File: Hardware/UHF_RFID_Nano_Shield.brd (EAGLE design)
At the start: 77.5 x 53.3 mm, 35 parts, among them J2 FTDI, J3 JST, J4 U.FL, J5 Extra, J6 Screw Terminal, J7 GPIOs, U1 Nano, U2 TXB0104, U3 TVS_DIODE_ARRAY

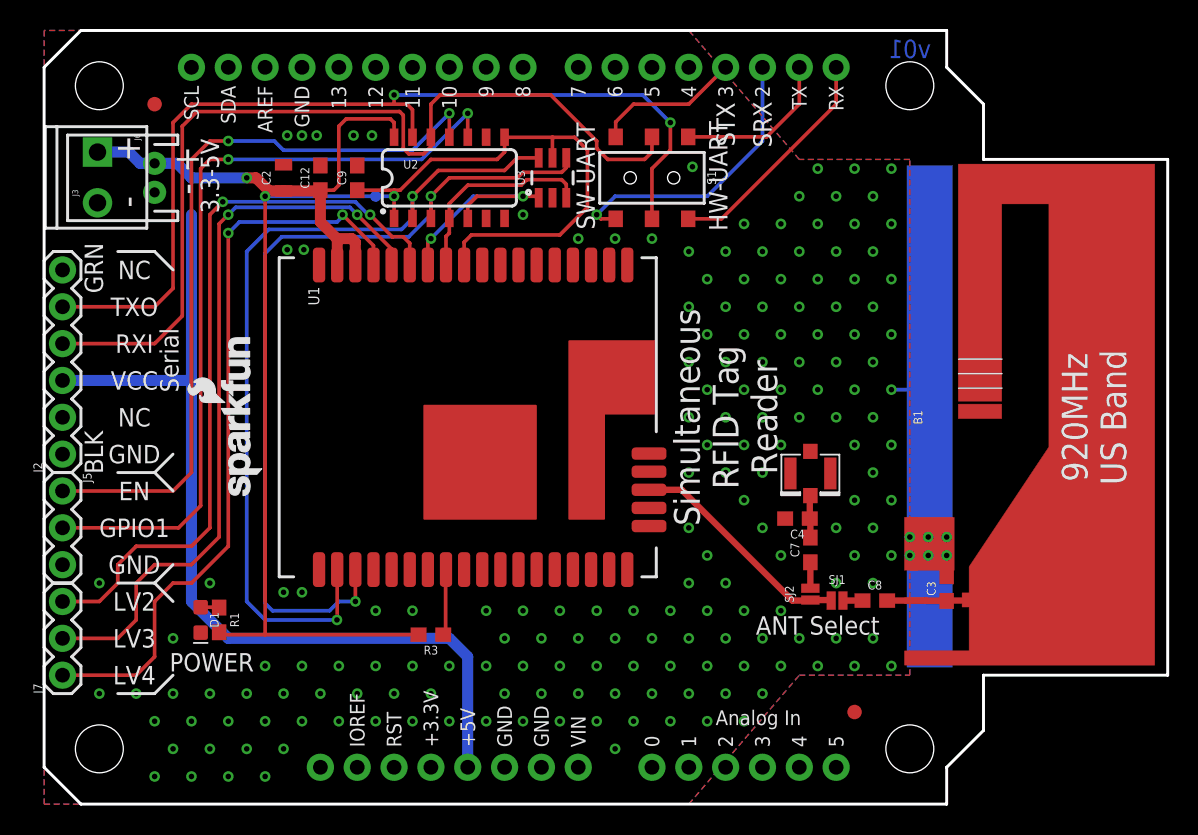
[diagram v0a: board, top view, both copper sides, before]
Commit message: Many changes from design review
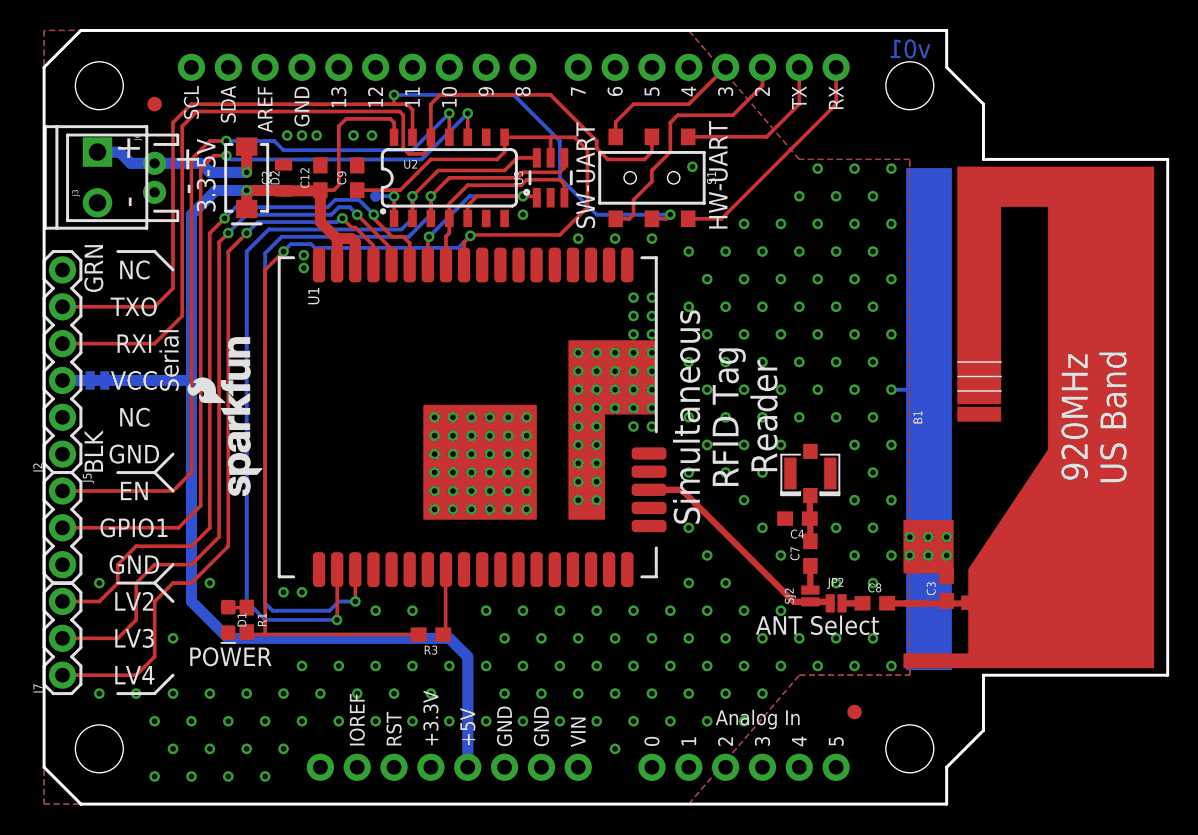
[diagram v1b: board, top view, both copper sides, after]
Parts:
- removed SJ1: (no value), SparkFun-Jumpers:SMT-JUMPER_2_NC_PASTE_NO-SILK
- added D2: 3A/40V/500mV, SparkFun-DiscreteSemi:SMA-DIODE
- added JP1: (no value), SparkFun-Jumpers:SMT-JUMPER_2_NC_TRACE_SILK
- added JP2: SJ1, SparkFun-Jumpers:SMT-JUMPER_2_NO_NO-SILK
- U3: value TVS_DIODE_ARRAY -> ESD Diode
- moved R1 1.91 mm to (14.0, 12.7)
- moved D1 1.90 mm to (12.7, 12.7)
- moved C7 0.25 mm to (52.8, 17.3)
- moved E2 0.20 mm to (59.4, 13.8)
- moved C8 0.19 mm to (57.3, 13.8)
- moved U3 0.13 mm to (34.9, 43.2)
- moved SJ2 0.13 mm to (52.8, 14.4)
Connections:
- new net N$12: D2.A, J3.2, J6.1
- new net N$7: J2.3, JP1.2
- net ANT3: now also JP2.1; no longer SJ1.1
- net N$2: now also JP2.2; no longer SJ1.2
- net VCC: now also D2.C, JP1.1; no longer J2.3, J3.2, J6.1
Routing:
- net N$12: track 0.00 -> 12.6 mm, vias 0 -> 1
- net VCC: track 99.5 -> 91.0 mm
- net SOFT-RX: track 20.0 -> 17.4 mm, vias 1 -> 0
- net N$7: track 0.00 -> 1.90 mm
- net TXO: track 66.3 -> 64.6 mm
- net GPIO4-LV: track 51.8 -> 50.9 mm
- net N$10: track 0.00 -> 0.76 mm
- net GPIO3-LV: track 51.4 -> 50.7 mm
- net 3.3V: track 89.7 -> 90.4 mm, vias 2 -> 3
- net GND: track 9.40 -> 9.69 mm, vias 184 -> 257
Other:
- board text added: "JP1"
- board text removed: "SRX"
- board text removed: "STX"
